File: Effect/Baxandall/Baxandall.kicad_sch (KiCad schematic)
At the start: 27 parts, among them J1 Conn_01x04_Pin, J2 Conn_01x03_Pin, U1 OPA1656

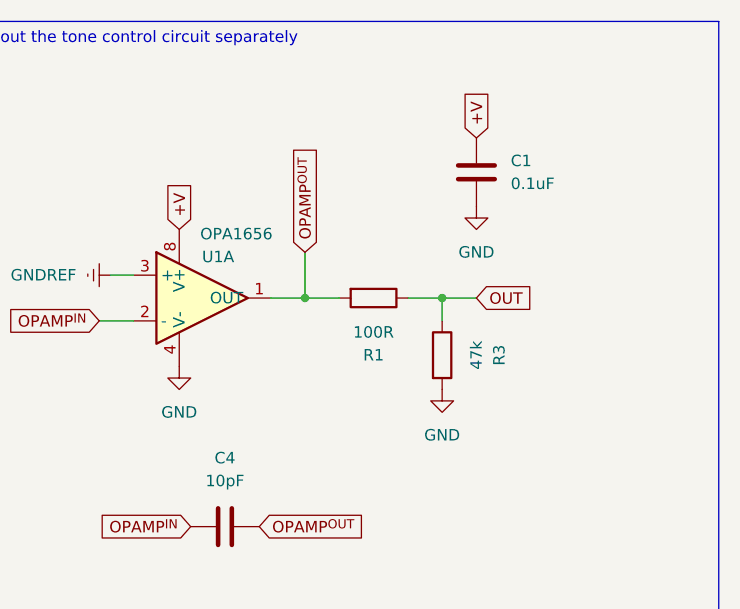
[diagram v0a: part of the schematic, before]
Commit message: Baxandall: remove unnecessary output resistors
These came from the TI reference design, and I kept them around until I
actually put the board together, at which point I went "I like the
tinkering, but not pointlessly".

So remove them.

I'm not sure why that 47kΩ resistor to ground was there.  As some kind
of preemptive DC biasing for the next stage with a capacitive input? Not
relevant for this design.

Signed-off-by: Linus Torvalds <torvalds@linux-foundation.org>
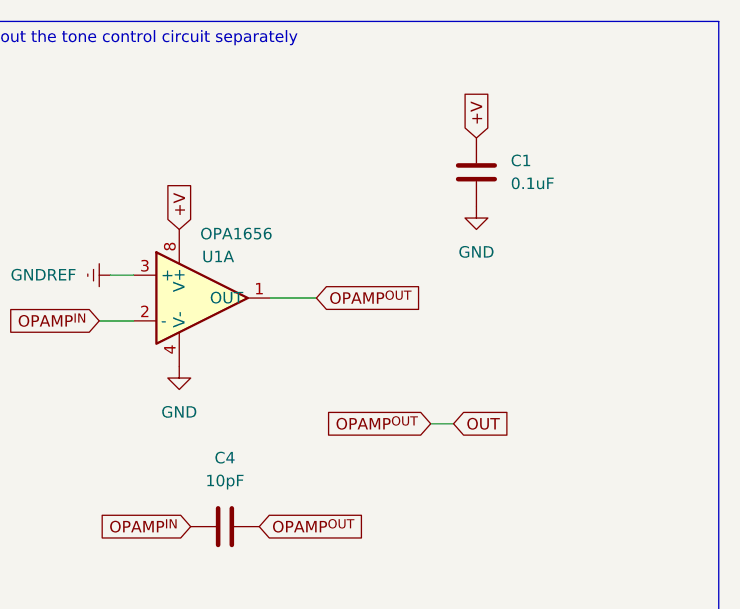
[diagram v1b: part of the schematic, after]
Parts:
- removed R1: 100R, Resistor_SMD:R_0805_2012Metric_Pad1.20x1.40mm_HandSolder, symbol Device:R
- removed R3: 47k, Resistor_SMD:R_0805_2012Metric_Pad1.20x1.40mm_HandSolder, symbol Device:R
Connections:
- net OUT is gone; now on net OPAMP^{OUT}: J2.2 (Pin_2)
